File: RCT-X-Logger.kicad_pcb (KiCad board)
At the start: 2 copper layers, 30 x 70 mm, 66 parts, among them J1 USB_B_Micro, P1 KRC_Conn_SWD, U1 KRC_Conn_CAN, U2 LT1761-5, U3 LT1965xDD-3.3, U4 NCV7342, U5 CY8C58xxLTI-LPxxx, U6 CAM-M8C, U7 MS5607, U8 W25N01GVxxIG-IT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

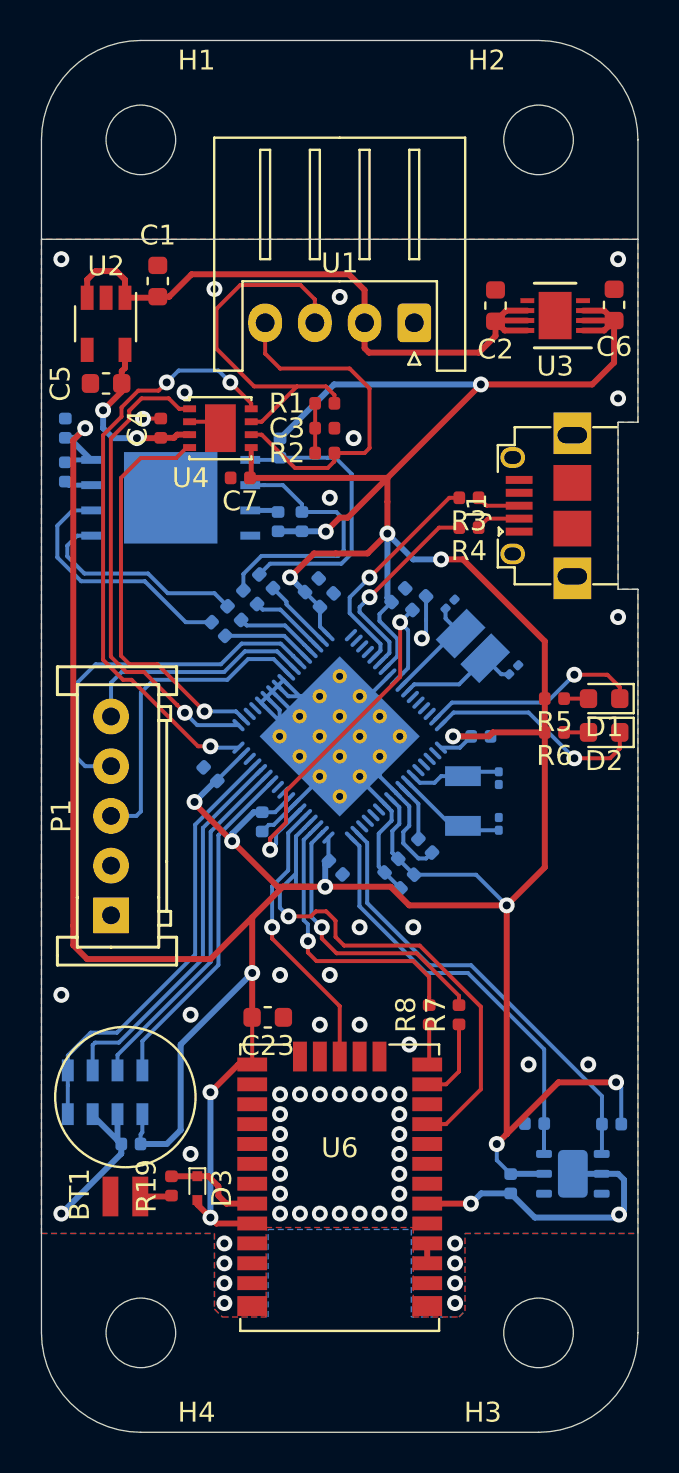
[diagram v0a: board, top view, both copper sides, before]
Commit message: [add]wrote pin asign and logo
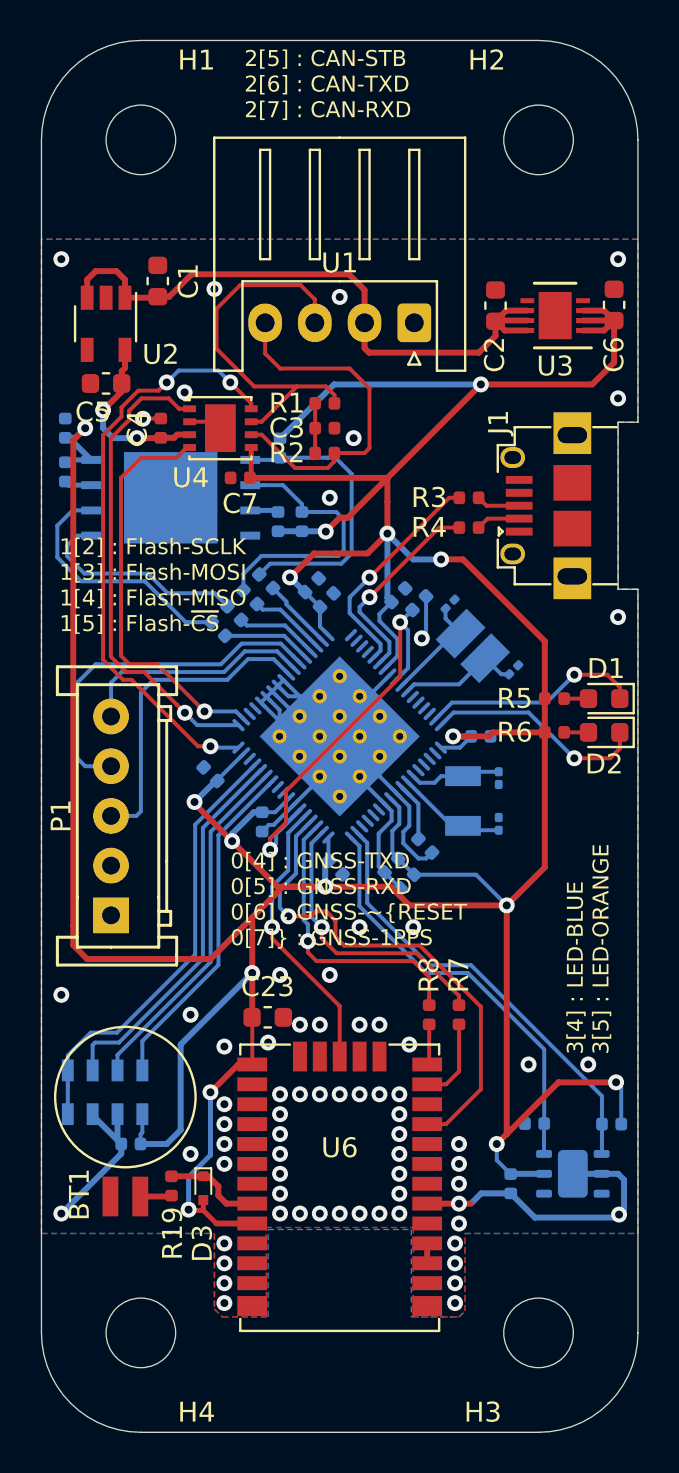
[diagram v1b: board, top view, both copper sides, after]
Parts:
- added G***: LOGO, KUTKiCad_footprint:yuru, B.Cu at (63.2, 75.2)
- added G***: LOGO, KUTKiCad_footprint:logo, B.Cu at (62.6, 71.0)
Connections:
- U3 pad 9: (no net) -> GND
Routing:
- net /GNSS-~RESET: track 27.9 -> 25.5 mm
- net +3V3: track 240.6 -> 241.3 mm
- net GND: vias 58 -> 70
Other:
- outline, holes or cut-outs redrawn
- board text added: "0[2] : H-SDA 0[3] : H-SCL"
- board text added: "0[4] : GNSS-TXD 0[5] : GNSS-RXD 0[6] : GNSS-~RESET 0[7] : GNSS-1PPS"
- board text added: "0[4] : GNSS-TXD 0[5] : GNSS-RXD 0[6] : GNSS-~RESET 0[7] : GNSS-1PPS 1[2] : Flash-SCLK 1[3] : Flash-MOSI 1[4] : Flash-MISO 1[5] : Flash-~CS 2[0] : PT-SCLK 2[1] : PT-MOSI 2[2] : PT-MISO 2[3] : PT-~CS"
- board text added: "1[2] : Flash-SCLK 1[3] : Flash-MOSI 1[4] : Flash-MISO 1[5] : Flash-~CS"
- board text added: "2[0] : PT-SCLK 2[1] : PT-MOSI 2[2] : PT-MISO 2[3] : PT-~CS"
- board text added: "2[5] : CAN-STB 2[6] : CAN-TXD 2[7] : CAN-RXD"
- board text added: "3[4] : LED-BLUE 3[5] : LED-ORANGE"
- board text added: "Rev1.0.0"
